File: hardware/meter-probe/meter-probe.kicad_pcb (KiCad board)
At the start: 4 copper layers, 40 x 68 mm, 57 parts, among them J1 Cable, SW1 Sensor Button, U1 TSL2522, U2 USBLC6-2SC6, U3 MIC5365-1.8YC5, U4 FT260Q, U5 CAT24C08

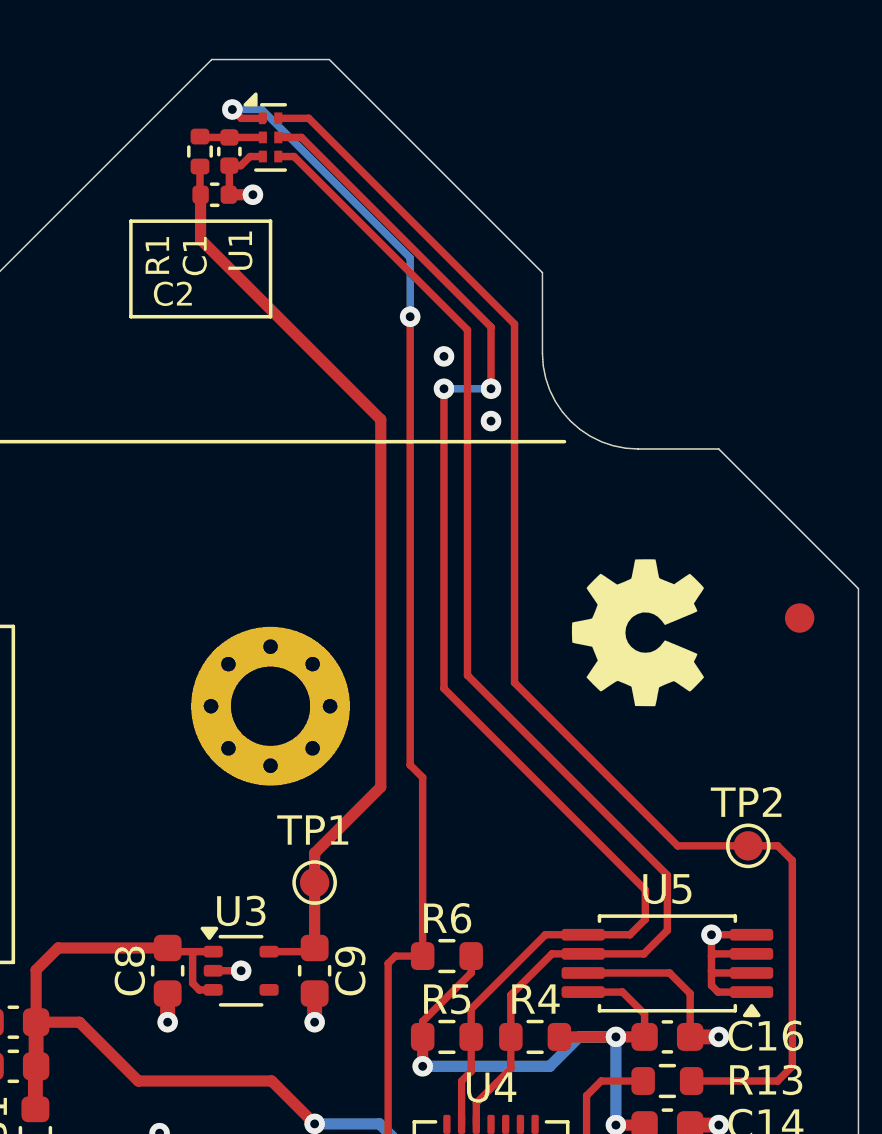
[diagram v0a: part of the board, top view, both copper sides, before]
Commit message: Fix sensor footprint on meter probe
Ideally this fix should also be applied to the DensiStick, but that
should only happen if another run of PCBs are produced for that layout.
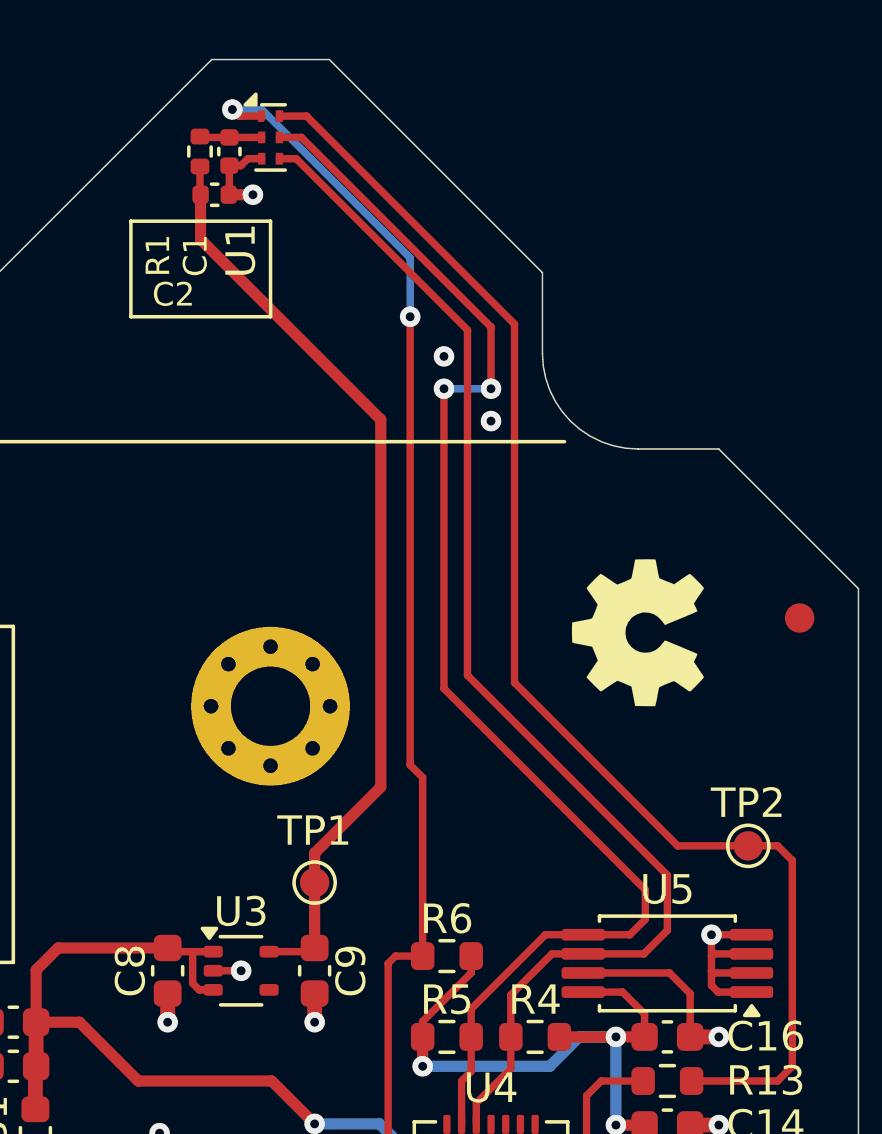
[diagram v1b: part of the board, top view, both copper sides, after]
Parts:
- U1: footprint lib_fp:AMS_TSL2585_OLGA-6_2x1mm_P0.65mm -> lib_fp:AMS_TSL2522_OLGA-6_2x1mm_P0.65mm

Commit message: Updates to help with PCB assembly concerns
Added panelization tab indicator
Added fourth fiducial, and enabled lock attribute on all fiducials
Updated pcb/schematic dates
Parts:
- added FID4: Fiducial, Fiducial:Fiducial_1mm_Mask2mm, F.Cu at (113.0, 70.0)
- added REF**: Tab, PCM_kikit:Tab, F.Cu at (99.5, 88.0)
- added REF**: Tab, PCM_kikit:Tab, F.Cu at (140.5, 88.0)
- moved REF** 20.0 mm to (140.5, 118.0)
- moved REF** 20.0 mm to (99.5, 118.0)
